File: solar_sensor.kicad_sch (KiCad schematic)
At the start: 3 parts

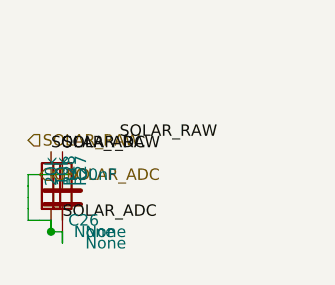
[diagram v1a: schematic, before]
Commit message: fix router map cell no more mark for pins
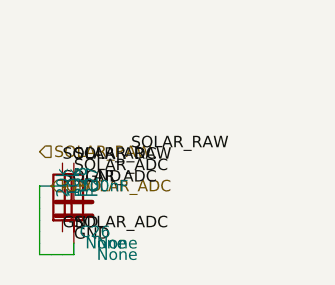
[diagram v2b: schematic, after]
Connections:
- net GND: now also C26.1

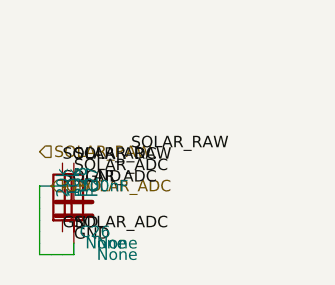
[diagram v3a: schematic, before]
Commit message: исправлены метки
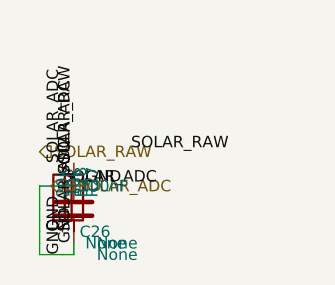
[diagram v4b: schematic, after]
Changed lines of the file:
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@@
 		(instances
 			(project "Untitled"
-				(path "/96a8192d-f339-430d-a0df-5a5e4e037b8c"
+				(path "/409c93fd-bba0-4dd0-8760-a3cdb1c560b2"
 					(reference "C26")
 					(unit 1)
@@
 		(instances
 			(project "Untitled"
-				(path "/96a8192d-f339-430d-a0df-5a5e4e037b8c"
+				(path "/409c93fd-bba0-4dd0-8760-a3cdb1c560b2"
 					(reference "R27")
 					(unit 1)
@@
 		(instances
 			(project "Untitled"
-				(path "/96a8192d-f339-430d-a0df-5a5e4e037b8c"
+				(path "/409c93fd-bba0-4dd0-8760-a3cdb1c560b2"
 					(reference "R28")
 					(unit 1)
@@
 	)
 	(label "GND"
-		(at 16.51 21.59 0)
-		(effects
-			(font
-				(size 1.27 1.27)
-			)
-			(justify left bottom)
-		)
-	)
-	(label "GND"
-		(at 17.78 22.86 0)
-		(effects
-			(font
-				(size 1.27 1.27)
-			)
-			(justify left bottom)
-		)
-	)
-	(label "GND"
-		(at 19.05 16.51 0)
+		(at 16.51 21.59 270)
+		(effects
+			(font
+				(size 1.27 1.27)
+			)
+			(justify left bottom)
+		)
+	)
+	(label "GND"
+		(at 17.78 22.86 270)
+		(effects
+			(font
+				(size 1.27 1.27)
+			)
+			(justify left bottom)
+		)
+	)
+	(label "GND"
+		(at 19.05 16.51 180)
+		(effects
+			(font
+				(size 1.27 1.27)
+			)
+			(justify left bottom)
+		)
+	)
+	(label "GND"
+		(at 16.51 24.13 270)
 		(effects
 			(font
@@
 	)
 	(label "SOLAR_RAW"
-		(at 17.78 13.97 0)
+		(at 17.78 13.97 90)
 		(effects
 			(font
@@
 	)
 	(label "SOLAR_RAW"
-		(at 24.13 12.7 0)
-		(effects
-			(font
-				(size 1.27 1.27)
-			)
-			(justify left bottom)
-		)
-	)
-	(label "SOLAR_ADC"
-		(at 16.51 13.97 0)
-		(effects
-			(font
-				(size 1.27 1.27)
-			)
-			(justify left bottom)
-		)
-	)
-	(label "SOLAR_ADC"
-		(at 17.78 15.24 0)
-		(effects
-			(font
-				(size 1.27 1.27)
-			)
-			(justify left bottom)
-		)
-	)
-	(label "SOLAR_ADC"
-		(at 16.51 16.51 0)
-		(effects
-			(font
-				(size 1.27 1.27)
-			)
-			(justify left bottom)
-		)
-	)
-	(label "SOLAR_ADC"
-		(at 17.78 21.59 0)
-		(effects
-			(font
+		(at 24.13 12.7 180)
+		(effects
+			(font
+				(size 1.27 1.27)
+			)
+			(justify left bottom)
+		)
+	)
+	(label "SOLAR_ADC"
+		(at 16.51 13.97 90)
+		(effects
+			(font
+				(size 1.27 1.27)
+			)
+			(justify left bottom)
+		)
+	)
+	(label "SOLAR_ADC"
+		(at 17.78 15.24 90)
+		(effects
+			(font
+				(size 1.27 1.27)
+			)
+			(justify left bottom)
+		)
+	)
+	(label "SOLAR_ADC"
+		(at 16.51 16.51 0.0000)
+		(effects
+			(font
+				(size 1.27 1.27)
+			)
+			(justify left bottom)
+		)
+	)
+	(label "SOLAR_ADC"
+		(at 17.78 21.59 270)
+		(effects
+			(font

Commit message: fix writer
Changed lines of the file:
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@@
 		(instances
 			(project "Untitled"
-				(path "/409c93fd-bba0-4dd0-8760-a3cdb1c560b2"
+				(path "/232a395d-dcd7-4c92-b9dd-1bda61371bf3"
 					(reference "C26")
 					(unit 1)
@@
 		(instances
 			(project "Untitled"
-				(path "/409c93fd-bba0-4dd0-8760-a3cdb1c560b2"
+				(path "/232a395d-dcd7-4c92-b9dd-1bda61371bf3"
 					(reference "R27")
 					(unit 1)
@@
 		(instances
 			(project "Untitled"
-				(path "/409c93fd-bba0-4dd0-8760-a3cdb1c560b2"
+				(path "/232a395d-dcd7-4c92-b9dd-1bda61371bf3"
 					(reference "R28")
 					(unit 1)
@@
 	(wire
 		(pts
-			(xy 17.78 24.13) (xy 16.51 24.13)
-		)
-		(stroke
-			(width 0)
-			(type default)
-		)
-	)
-	(wire
-		(pts
-			(xy 16.51 24.13) (xy 15.24 24.13)
-		)
-		(stroke
-			(width 0)
-			(type default)
-		)
-	)
-	(wire
-		(pts
-			(xy 15.24 24.13) (xy 13.97 24.13)
-		)
-		(stroke
-			(width 0)
-			(type default)
-		)
-	)
-	(wire
-		(pts
-			(xy 13.97 24.13) (xy 13.97 22.86)
-		)
-		(stroke
-			(width 0)
-			(type default)
-		)
-	)
-	(wire
-		(pts
-			(xy 13.97 22.86) (xy 13.97 21.59)
-		)
-		(stroke
-			(width 0)
-			(type default)
-		)
-	)
-	(wire
-		(pts
-			(xy 13.97 21.59) (xy 13.97 20.32)
-		)
-		(stroke
-			(width 0)
-			(type default)
-		)
-	)
-	(wire
-		(pts
-			(xy 13.97 20.32) (xy 13.97 19.05)
-		)
-		(stroke
-			(width 0)
-			(type default)
-		)
-	)
-	(wire
-		(pts
-			(xy 13.97 19.05) (xy 13.97 17.78)
-		)
-		(stroke
-			(width 0)
-			(type default)
-		)
-	)
-	(wire
-		(pts
-			(xy 13.97 17.78) (xy 13.97 16.51)
+			(xy 17.78 24.13) (xy 13.97 24.13)
+		)
+		(stroke
+			(width 0)
+			(type default)
+		)
+	)
+	(wire
+		(pts
+			(xy 13.97 24.13) (xy 13.97 16.51)
 		)
 		(stroke
@@
 	(hierarchical_label "GND"
 		(shape input)
-		(at 15.24 16.51 180)
+		(at 19.05 16.51 180)
 		(effects
 			(font
@@
 	(hierarchical_label "SOLAR_RAW"
 		(shape input)
-		(at 13.97 12.7 180)
-		(effects
-			(font
+		(at 24.13 12.7 180)
+		(effects
+			(font

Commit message: fic placer for small schemes
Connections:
- net GND: no longer C26.1, R27.2, R28.1
- new net SOLAR_ADC: C26.1, R27.2, R28.1
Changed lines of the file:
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@@
 	(symbol
 		(lib_id "Device:C")
-		(at 17.78 19.05 0)
+		(at 17.78 15.24 0)
 		(unit 1)
 		(exclude_from_sim no)
@@
 		(fields_autoplaced no)
 		(property "Reference" "C26"
-			(at 18.415 21.59 0.0000)
+			(at 18.415 17.78 0.0000)
 			(effects
 				(font
@@
 		)
 		(property "Value" "100nF"
-			(at 18.415 16.51 0.0000)
+			(at 18.415 12.7 0.0000)
 			(effects
 				(font
@@
 		)
 		(property "mirror" "None"
-			(at 20.32 24.1299 0)
+			(at 20.32 20.3199 0)
 			(effects
 				(font
@@
 		(instances
 			(project "Untitled"
-				(path "/0db772c6-c8f2-4d81-8602-14e856cc1f5d"
+				(path "/1fbe9de3-9289-44a8-9734-4d68a48c9c9d"
 					(reference "C26")
 					(unit 1)
@@
 	(symbol
 		(lib_id "Device:R")
-		(at 17.78 17.78 0)
+		(at 21.59 15.24 0)
 		(unit 1)
 		(exclude_from_sim no)
@@
 		(fields_autoplaced no)
 		(property "Reference" "R27"
-			(at 19.812 17.78 90)
+			(at 23.622 15.24 90)
 			(effects
 				(font
@@
 		)
 		(property "Value" "10k"
-			(at 17.78 17.78 90)
+			(at 21.59 15.24 90)
 			(effects
 				(font
@@
 		)
 		(property "mirror" "None"
-			(at 20.32 22.8599 0)
+			(at 24.13 20.3199 0)
 			(effects
 				(font
@@
 		(instances
 			(project "Untitled"
-				(path "/0db772c6-c8f2-4d81-8602-14e856cc1f5d"
+				(path "/1fbe9de3-9289-44a8-9734-4d68a48c9c9d"
 					(reference "R27")
 					(unit 1)
@@
 	(symbol
 		(lib_id "Device:R")
-		(at 16.51 17.78 0)
+		(at 13.97 15.24 0)
 		(unit 1)
 		(exclude_from_sim no)
@@
 		(fields_autoplaced no)
 		(property "Reference" "R28"
-			(at 18.542 17.78 90)
+			(at 16.002 15.24 90)
 			(effects
 				(font
@@
 		)
 		(property "Value" "20k"
-			(at 16.51 17.78 90)
+			(at 13.97 15.24 90)
 			(effects
 				(font
@@
 		)
 		(property "mirror" "None"
-			(at 19.05 22.8599 0)
+			(at 16.51 20.3199 0)
 			(effects
 				(font
@@
 		(instances
 			(project "Untitled"
-				(path "/0db772c6-c8f2-4d81-8602-14e856cc1f5d"
+				(path "/1fbe9de3-9289-44a8-9734-4d68a48c9c9d"
 					(reference "R28")
 					(unit 1)
@@
 	(wire
 		(pts
-			(xy 17.78 22.86) (xy 17.78 24.13)
-		)
-		(stroke
-			(width 0)
-			(type default)
-		)
-	)
-	(wire
-		(pts
-			(xy 17.78 24.13) (xy 13.97 24.13)
-		)
-		(stroke
-			(width 0)
-			(type default)
-		)
-	)
-	(wire
-		(pts
-			(xy 13.97 24.13) (xy 13.97 16.51)
-		)
-		(stroke
-			(width 0)
-			(type default)
-		)
-	)
-	(wire
-		(pts
-			(xy 13.97 16.51) (xy 19.05 16.51)
-		)
-		(stroke
-			(width 0)
-			(type default)
-		)
+			(xy 13.97 11.43) (xy 13.97 10.16)
+		)
+		(stroke
+			(width 0)
+			(type default)
+		)
+	)
+	(wire
+		(pts
+			(xy 13.97 10.16) (xy 17.78 10.16)
+		)
+		(stroke
+			(width 0)
+			(type default)
+		)
+	)
+	(wire
+		(pts
+			(xy 17.78 10.16) (xy 17.78 11.43)
+		)
+		(stroke
+			(width 0)
+			(type default)
+		)
+	)
+	(wire
+		(pts
+			(xy 17.78 20.32) (xy 29.21 20.32)
+		)
+		(stroke
+			(width 0)
+			(type default)
+		)
+	)
+	(wire
+		(pts
+			(xy 29.21 20.32) (xy 31.75 20.32)
+		)
+		(stroke
+			(width 0)
+			(type default)
+		)
+	)
+	(wire
+		(pts
+			(xy 31.75 20.32) (xy 31.75 7.62)
+		)
+		(stroke
+			(width 0)
+			(type default)
+		)
+	)
+	(wire
+		(pts
+			(xy 31.75 7.62) (xy 17.78 7.62)
+		)
+		(stroke
+			(width 0)
+			(type default)
+		)
+	)
+	(wire
+		(pts
+			(xy 17.78 7.62) (xy 17.78 10.16)
+		)
+		(stroke
+			(width 0)
+			(type default)
+		)
+	)
+	(junction
+		(at 17.78 10.16)
+		(diameter 0)
+		(color 0 0 0 0)
 	)
 	(label "GND"
-		(at 16.51 21.59 270)
+		(at 17.78 19.05 270)
 		(effects
 			(font
@@
 	)
 	(label "GND"
-		(at 17.78 22.86 270)
+		(at 16.51 20.32 180)
 		(effects
 			(font
@@
 	)
 	(label "GND"
-		(at 19.05 16.51 180)
-		(effects
-			(font
-				(size 1.27 1.27)
-			)
-			(justify left bottom)
-		)
-	)
-	(label "GND"
-		(at 16.51 24.13 270)
+		(at 13.97 19.05 270)
 		(effects
 			(font
@@
 	)
 	(label "SOLAR_RAW"
-		(at 17.78 13.97 90)
+		(at 21.59 11.43 90)
 		(effects
 			(font
@@
 	)
 	(label "SOLAR_RAW"
-		(at 24.13 12.7 180)
+		(at 30.48 8.89 180)
 		(effects
 			(font
@@
 	)
 	(label "SOLAR_ADC"
-		(at 16.51 13.97 90)
+		(at 21.59 19.05 270)
 		(effects
 			(font
@@
 	)
 	(label "SOLAR_ADC"
-		(at 17.78 15.24 90)
-		(effects
-			(font
-				(size 1.27 1.27)
-			)
-			(justify left bottom)
-		)
-	)
-	(label "SOLAR_ADC"
-		(at 16.51 16.51 0.0000)
-		(effects
-			(font
-				(size 1.27 1.27)
-			)
-			(justify left bottom)
-		)
-	)
-	(label "SOLAR_ADC"
-		(at 17.78 21.59 270)
+		(at 17.78 10.16 270)
 		(effects
 			(font
@@
 	(hierarchical_label "GND"
 		(shape input)
-		(at 19.05 16.51 180)
+		(at 16.51 20.32 180)
 		(effects
 			(font
@@
 	(hierarchical_label "SOLAR_RAW"
 		(shape input)
-		(at 24.13 12.7 180)
+		(at 30.48 8.89 180)
 		(effects
 			(font
@@
 	(hierarchical_label "SOLAR_ADC"
 		(shape input)
-		(at 16.51 16.51 0)
-		(effects
-			(font
+		(at 17.78 20.32 0)
+		(effects
+			(font
